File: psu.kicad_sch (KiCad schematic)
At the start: 4 parts, among them U2 XC6220B331MR

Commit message: initial commit, not complete.
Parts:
- C10: footprint Capacitor_SMD:C_0805_2012Metric -> Capacitor_SMD:C_0805_2012Metric_Pad1.18x1.45mm_HandSolder
- C11, C13: footprint Capacitor_SMD:C_0402_1005Metric -> Capacitor_SMD:C_0603_1608Metric_Pad1.08x0.95mm_HandSolder
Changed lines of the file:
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@@
 			)
 		)
-		(property "Footprint" "Capacitor_SMD:C_0805_2012Metric"
+		(property "Footprint" "Capacitor_SMD:C_0805_2012Metric_Pad1.18x1.45mm_HandSolder"
 			(at 133.35 99.06 0)
 			(effects
@@
 			)
 		)
-		(property "Footprint" "Capacitor_SMD:C_0402_1005Metric"
+		(property "Footprint" "Capacitor_SMD:C_0603_1608Metric_Pad1.08x0.95mm_HandSolder"
 			(at 119.38 99.06 0)
 			(effects
@@
 			)
 		)
-		(property "Footprint" "Capacitor_SMD:C_0402_1005Metric"
+		(property "Footprint" "Capacitor_SMD:C_0603_1608Metric_Pad1.08x0.95mm_HandSolder"
 			(at 172.72 99.06 0)
 			(effects

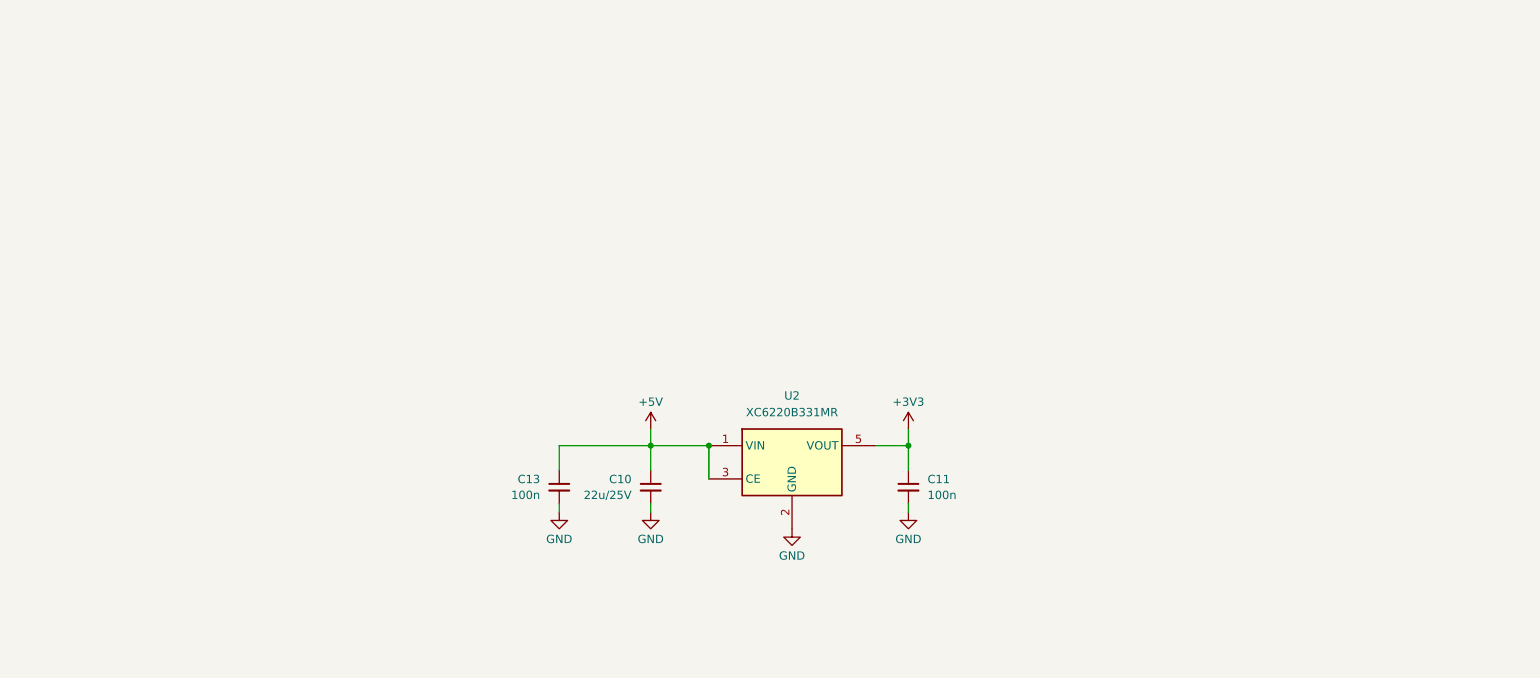
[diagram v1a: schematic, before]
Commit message: PCB shape is created. Most of routing done.
Todo: assign pins for radio control signals.
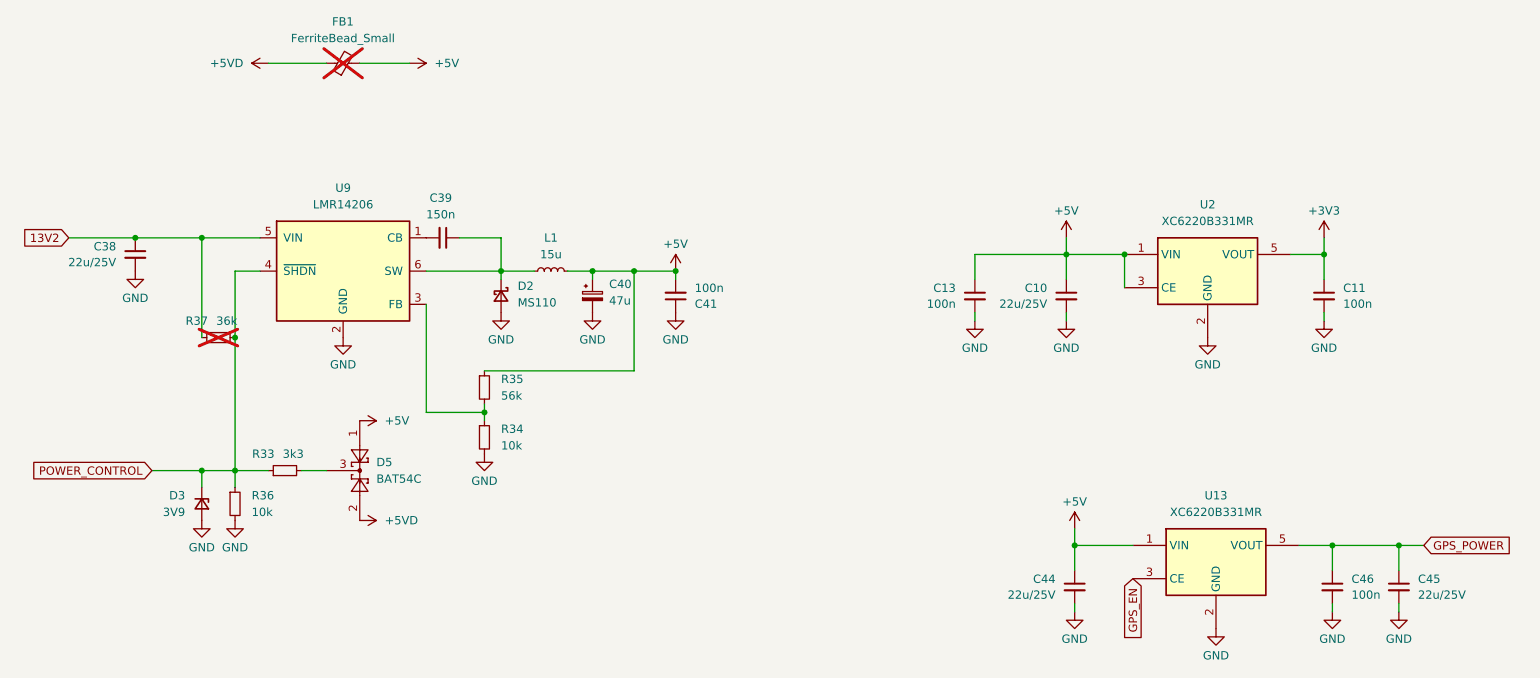
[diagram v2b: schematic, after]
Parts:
- added C38, C44, C45: 22u/25V, Capacitor_SMD:C_0805_2012Metric_Pad1.18x1.45mm_HandSolder, symbol Device:C_Small
- added C39: 150n, Capacitor_SMD:C_0603_1608Metric_Pad1.08x0.95mm_HandSolder, symbol Device:C_Small
- added C40: 47u, Capacitor_SMD:C_0805_2012Metric, symbol Device:C_Polarized_Small
- added C41, C46: 100n, Capacitor_SMD:C_0603_1608Metric_Pad1.08x0.95mm_HandSolder, symbol Device:C_Small
- added D2: MS110, Diode_SMD:D_SMA, symbol Device:D_Schottky_Small
- added D3: 3V9, Diode_SMD:D_SOD-323_HandSoldering, symbol Device:D_Zener_Small
- added D5: BAT54C, Package_TO_SOT_SMD:SOT-23, symbol Diode:BAT54C
- added FB1: FerriteBead_Small, Inductor_SMD:L_0805_2012Metric_Pad1.15x1.40mm_HandSolder, symbol Device:FerriteBead_Small
- added L1: 15u, Inductor_SMD:L_Bourns-SRN6028, symbol Device:L_Small
- added R33: 3k3, Resistor_SMD:R_0603_1608Metric_Pad0.98x0.95mm_HandSolder, symbol Device:R_Small
- added R34, R36: 10k, Resistor_SMD:R_0603_1608Metric_Pad0.98x0.95mm_HandSolder, symbol Device:R_Small
- added R35: 56k, Resistor_SMD:R_0603_1608Metric_Pad0.98x0.95mm_HandSolder, symbol Device:R_Small
- added R37: 36k, Resistor_SMD:R_0603_1608Metric_Pad0.98x0.95mm_HandSolder, symbol Device:R_Small
- added U13: XC6220B331MR, Package_TO_SOT_SMD:SOT-23-5, symbol Regulator_Linear:XC6220B331MR
- added U9: LMR14206, Package_TO_SOT_SMD:SOT-23-6, symbol Regulator_Switching:LMR14206
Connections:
- net +5V: now also C40.1, C41.2, C44.1, D5.1, FB1.2, L1.2, R35.1, U13.1 (VIN)
- net GND: now also C38.2, C40.2, C41.1, C44.2, C45.2, C46.2, D2.2 (A), D3.2 (A), R34.2, R36.2, U13.2 (GND), U9.2 (GND)
- new net: D5.3, R33.2
- new net: R34.1, R35.2, U9.3 (FB)
- new net: C39.1, D2.1 (K), L1.1, U9.6 (SW)
- new net: C39.2, U9.1 (CB)
- new net +5VD: D5.2, FB1.1
- new net 13V2: C38.1, R37.1, U9.5 (VIN)
- new net GPS_EN: U13.3 (CE)
- new net GPS_POWER: C45.1, C46.1, U13.5 (VOUT)
- new net POWER_CONTROL: D3.1 (K), R33.1, R36.1, R37.2, U9.4 (~{SHDN})
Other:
- moved on the sheet: C10, C11, C13, U2
